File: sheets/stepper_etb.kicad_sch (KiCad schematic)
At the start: 12 parts, among them U202 DRV8825PWPR, U203 TLE9201SG

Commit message: Remediate power supply, main relay keep-alive, and schematic ERC to 0 errors
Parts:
- added D209: B340A-13-F, Diode_SMD:D_SMA, symbol Device:D_Schottky
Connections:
- net 12V_MR: now also D209.1 (K)
- net +3.3V renamed +3V3
- new net MAIN_RLY_CLAMP: D209.2 (A)
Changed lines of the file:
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@@
 		(dnp no)
 		(property "Reference" "#PWR0850" (at 48.26 38.1 0) (effects (font (size 1.27 1.27)) (hide yes)))
-		(property "Value" "+3.3V" (at 48.26 38.1 0) (effects (font (size 1.27 1.27))))
+		(property "Value" "+3V3" (at 48.26 38.1 0) (effects (font (size 1.27 1.27))))
 		(property "Footprint" "" (at 48.26 40.64 0) (effects (font (size 1.27 1.27)) (hide yes)))
 		(property "Datasheet" "" (at 48.26 40.64 0) (effects (font (size 1.27 1.27)) (hide yes)))
@@
 		(dnp no)
 		(property "Reference" "#PWR0851" (at 48.26 40.64 0) (effects (font (size 1.27 1.27)) (hide yes)))
-		(property "Value" "+3.3V" (at 48.26 40.64 0) (effects (font (size 1.27 1.27))))
+		(property "Value" "+3V3" (at 48.26 40.64 0) (effects (font (size 1.27 1.27))))
 		(property "Footprint" "" (at 48.26 43.18 0) (effects (font (size 1.27 1.27)) (hide yes)))
 		(property "Datasheet" "" (at 48.26 43.18 0) (effects (font (size 1.27 1.27)) (hide yes)))
@@
 		(dnp no)
 		(property "Reference" "#PWR0856" (at 74.93 99.05999999999999 0) (effects (font (size 1.27 1.27)) (hide yes)))
-		(property "Value" "+3.3V" (at 74.93 99.05999999999999 0) (effects (font (size 1.27 1.27))))
+		(property "Value" "+3V3" (at 74.93 99.05999999999999 0) (effects (font (size 1.27 1.27))))
 		(property "Footprint" "" (at 74.93 101.6 0) (effects (font (size 1.27 1.27)) (hide yes)))
 		(property "Datasheet" "" (at 74.93 101.6 0) (effects (font (size 1.27 1.27)) (hide yes)))
@@
 		(effects
 			(font
+				(size 1.27 1.27)
+			)
+			(justify left)
+		)
+	)
+	(symbol
+		(lib_id "Device:D_Schottky")
+		(at 139.7 111.76 0)
+		(unit 1)
+		(exclude_from_sim no)
+		(in_bom yes)
+		(on_board yes)
+		(dnp no)
+		(property "Reference" "D209" (at 139.7 109.22 0) (effects (font (size 1.27 1.27))))
+		(property "Value" "B340A-13-F" (at 139.7 114.3 0) (effects (font (size 1.27 1.27))))
+		(property "Footprint" "Diode_SMD:D_SMA" (at 139.7 111.76 0) (effects (font (size 1.27 1.27)) (hide yes)))
+		(property "LCSC" "C8598" (at 139.7 111.76 0) (effects (font (size 1.27 1.27)) (hide yes)))
+		(pin "1")
+		(pin "2")
+		(instances
+			(project "fome-mc" (path "/3b9c5ffd-e59b-402d-8c5e-052f7ca643a4/a1000000-0000-4000-8000-000000000002" (reference "D209") (unit 1)))
+		)
+	)
+	(wire
+		(pts
+			(xy 129.54 111.76) (xy 135.89 111.76)
+		)
+		(stroke
+			(width 0)
+			(type default)
+		)
+	)
+	(label "12V_MR"
+		(at 129.54 111.76 180)
+		(fields_autoplaced yes)
+		(effects
+			(font
+				(size 1.27 1.27)
+			)
+			(justify right bottom)
+		)
+	)
+	(wire
+		(pts
+			(xy 143.51 111.76) (xy 152.4 111.76)
+		)
+		(stroke
+			(width 0)
+			(type default)
+		)
+	)
+	(hierarchical_label "MAIN_RLY_CLAMP"
+		(shape passive)
+		(at 152.4 111.76 0)
+		(effects
+			(font

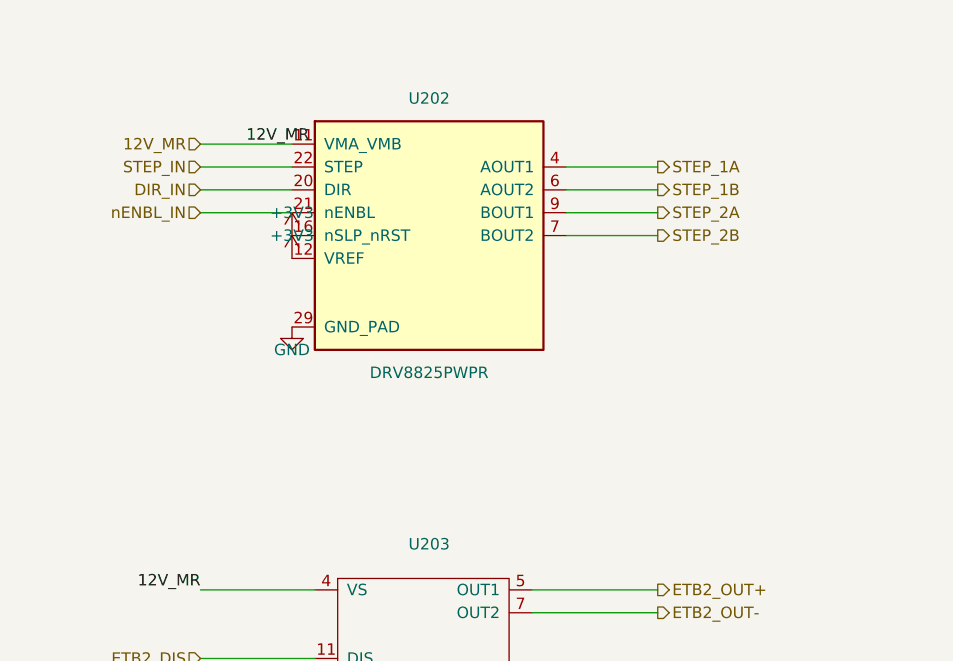
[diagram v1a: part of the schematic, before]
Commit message: Fix DRV8825PWPR (U202) HTSSOP-28 symbol pinout, VREF divider, charge pump, and 0.20R sense resistors (FOMEMC-5)
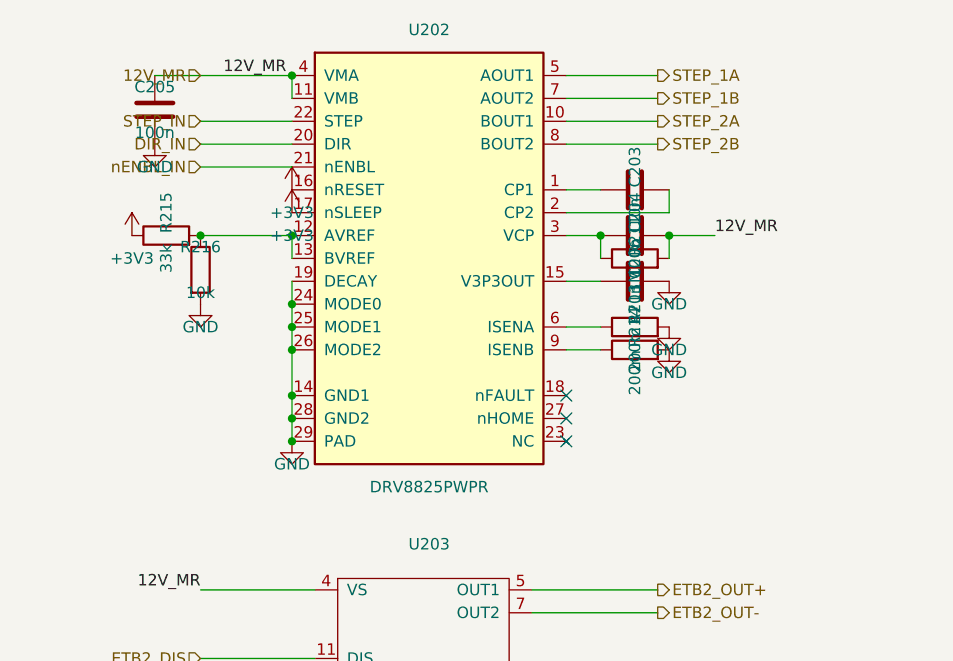
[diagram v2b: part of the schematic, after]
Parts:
- added C203: 10n, Capacitor_SMD:C_0603_1608Metric, symbol Device:C
- added C204, C205: 100n, Capacitor_SMD:C_0603_1608Metric, symbol Device:C
- added C206: 470n, Capacitor_SMD:C_0603_1608Metric, symbol Device:C
- added R211: 1M, Resistor_SMD:R_0603_1608Metric, symbol Device:R
- added R213, R214: 200m, Resistor_SMD:R_1206_3216Metric, symbol Device:R
- added R215: 33k, Resistor_SMD:R_0402_1005Metric, symbol Device:R
- added R216: 10k, Resistor_SMD:R_0402_1005Metric, symbol Device:R
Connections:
- net +3V3: now also U202.17 (nSLEEP), R215.1; no longer U202.12 (VREF)
- net 12V_MR: now also U202.4 (VMA), C204.2, C205.1, R211.2
- net GND: now also U202.14 (GND1), U202.19 (DECAY), U202.24 (MODE0), U202.25 (MODE1), U202.26 (MODE2), U202.28 (GND2), C205.2, C206.2, R213.2, R214.2, R216.2
- net STEP_1A: now also U202.5 (AOUT1); no longer U202.4 (AOUT1)
- net STEP_1B: now also U202.7 (AOUT2); no longer U202.6 (AOUT2)
- net STEP_2A: now also U202.10 (BOUT1); no longer U202.9 (BOUT1)
- net STEP_2B: now also U202.8 (BOUT2); no longer U202.7 (BOUT2)
- new net: R215.2, R216.1, U202.12 (AVREF), U202.13 (BVREF)
- new net: R214.1, U202.9 (ISENB)
- new net: C203.1, U202.1 (CP1)
- new net: C206.1, U202.15 (V3P3OUT)
- new net: C203.2, U202.2 (CP2)
- new net: C204.1, R211.1, U202.3 (VCP)
- new net: R213.1, U202.6 (ISENA)
- no-connect marks 4 -> 7

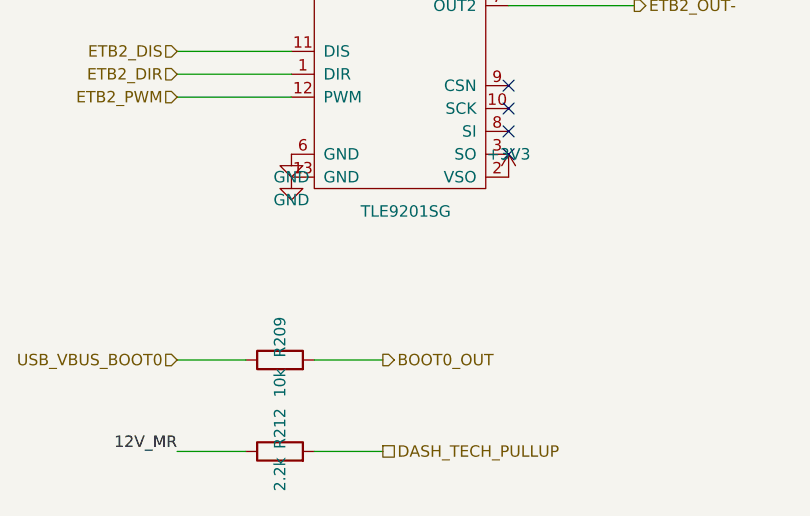
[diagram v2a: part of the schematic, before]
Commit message: Add D210 BZT52C6V8 BOOT0 threshold Zener, R217/R218/D211 PA9 VBUS sense divider/clamp, and SMCJ24A TVS protection on 12V_RAW and 12V_MR (FOMEMC-7)
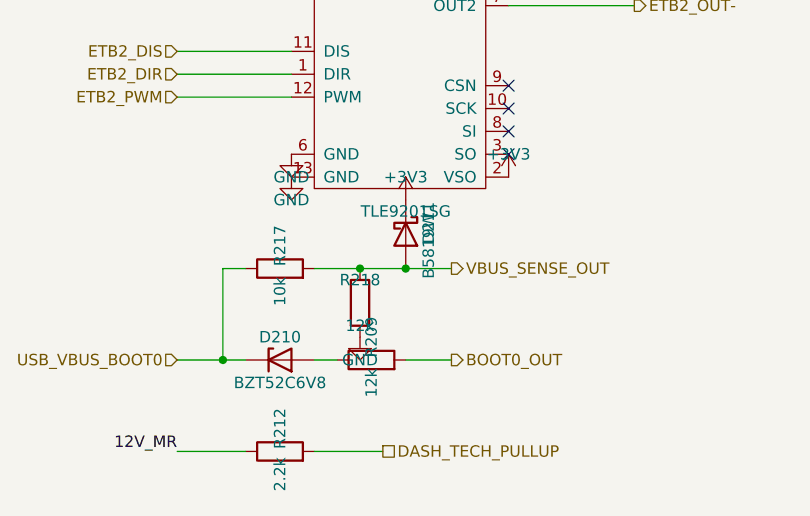
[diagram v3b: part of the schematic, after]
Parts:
- added D210: BZT52C6V8, Diode_SMD:D_SOD-123, symbol Device:D_Zener
- added D211: B5819W, Diode_SMD:D_SOD-123, symbol Device:D_Schottky
- added R217: 10k, Resistor_SMD:R_0402_1005Metric, symbol Device:R
- added R218: 12k, Resistor_SMD:R_0402_1005Metric, symbol Device:R
- R209: value 10k -> 12k; LCSC C25744 -> C25752
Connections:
- net +3V3: now also D211.1 (K)
- net GND: now also R218.2
- net USB_VBUS_BOOT0: now also D210.1 (K), R217.1; no longer R209.1
- new net: D210.2 (A), R209.1
- new net VBUS_SENSE_OUT: D211.2 (A), R217.2, R218.1
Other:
- moved on the sheet: R209
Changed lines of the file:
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@@
 	(wire
 		(pts
-			(xy 38.1 121.92) (xy 45.72 121.92)
+			(xy 38.1 121.92) (xy 43.18 121.92)
+		)
+		(stroke
+			(width 0)
+			(type default)
+		)
+	)
+	(wire
+		(pts
+			(xy 43.18 121.92) (xy 45.72 121.92)
+		)
+		(stroke
+			(width 0)
+			(type default)
+		)
+	)
+	(wire
+		(pts
+			(xy 43.18 121.92) (xy 43.18 111.76)
+		)
+		(stroke
+			(width 0)
+			(type default)
+		)
+	)
+	(wire
+		(pts
+			(xy 43.18 111.76) (xy 45.72 111.76)
+		)
+		(stroke
+			(width 0)
+			(type default)
+		)
+	)
+	(junction
+		(at 43.18 121.92)
+		(diameter 0)
+		(color 0 0 0 0)
+	)
+	(symbol
+		(lib_id "Device:D_Zener")
+		(at 49.53 121.92 0)
+		(unit 1)
+		(exclude_from_sim no)
+		(in_bom yes)
+		(on_board yes)
+		(dnp no)
+		(property "Reference" "D210" (at 49.53 119.38 0) (effects (font (size 1.27 1.27))))
+		(property "Value" "BZT52C6V8" (at 49.53 124.46 0) (effects (font (size 1.27 1.27))))
+		(property "Footprint" "Diode_SMD:D_SOD-123" (at 49.53 121.92 0) (effects (font (size 1.27 1.27)) (hide yes)))
+		(property "LCSC" "C173404" (at 49.53 121.92 0) (effects (font (size 1.27 1.27)) (hide yes)))
+		(pin "1")
+		(pin "2")
+		(instances
+			(project "fome-mc" (path "/3b9c5ffd-e59b-402d-8c5e-052f7ca643a4/a1000000-0000-4000-8000-000000000002" (reference "D210") (unit 1)))
+		)
+	)
+	(wire
+		(pts
+			(xy 53.34 121.92) (xy 55.88 121.92)
 		)
 		(stroke
@@
 	(symbol
 		(lib_id "Device:R")
-		(at 49.53 121.92 90)
-		(unit 1)
-		(exclude_from_sim no)
-		(in_bom yes)
-		(on_board yes)
-		(dnp no)
-		(property "Reference" "R209" (at 49.53 119.38 0) (effects (font (size 1.27 1.27))))
-		(property "Value" "10k" (at 49.53 124.46 0) (effects (font (size 1.27 1.27))))
-		(property "Footprint" "Resistor_SMD:R_0402_1005Metric" (at 49.53 121.92 0) (effects (font (size 1.27 1.27)) (hide yes)))
-		(property "LCSC" "C25744" (at 49.53 121.92 0) (effects (font (size 1.27 1.27)) (hide yes)))
+		(at 59.69 121.92 90)
+		(unit 1)
+		(exclude_from_sim no)
+		(in_bom yes)
+		(on_board yes)
+		(dnp no)
+		(property "Reference" "R209" (at 59.69 119.38 0) (effects (font (size 1.27 1.27))))
+		(property "Value" "12k" (at 59.69 124.46 0) (effects (font (size 1.27 1.27))))
+		(property "Footprint" "Resistor_SMD:R_0402_1005Metric" (at 59.69 121.92 0) (effects (font (size 1.27 1.27)) (hide yes)))
+		(property "LCSC" "C25752" (at 59.69 121.92 0) (effects (font (size 1.27 1.27)) (hide yes)))
 		(pin "1")
 		(pin "2")
 		(instances
 			(project "fome-mc" (path "/3b9c5ffd-e59b-402d-8c5e-052f7ca643a4/a1000000-0000-4000-8000-000000000002" (reference "R209") (unit 1)))
-			(project "fome-mc" (path "/3b9c5ffd-e59b-402d-8c5e-052f7ca643a4/a1000000-0000-4000-8000-000000000002" (reference "R209") (unit 1)))
-		)
-	)
-	(wire
-		(pts
-			(xy 53.34 121.92) (xy 60.96 121.92)
+		)
+	)
+	(wire
+		(pts
+			(xy 63.5 121.92) (xy 68.58 121.92)
 		)
 		(stroke
@@
 	(hierarchical_label "BOOT0_OUT"
 		(shape output)
-		(at 60.96 121.92 0)
+		(at 68.58 121.92 0)
 		(effects
 			(font
+				(size 1.27 1.27)
+			)
+			(justify left)
+		)
+	)
+	(symbol
+		(lib_id "Device:R")
+		(at 49.53 111.76 90)
+		(unit 1)
+		(exclude_from_sim no)
+		(in_bom yes)
+		(on_board yes)
+		(dnp no)
+		(property "Reference" "R217" (at 49.53 109.22 0) (effects (font (size 1.27 1.27))))
+		(property "Value" "10k" (at 49.53 114.3 0) (effects (font (size 1.27 1.27))))
+		(property "Footprint" "Resistor_SMD:R_0402_1005Metric" (at 49.53 111.76 0) (effects (font (size 1.27 1.27)) (hide yes)))
+		(property "LCSC" "C25744" (at 49.53 111.76 0) (effects (font (size 1.27 1.27)) (hide yes)))
+		(pin "1")
+		(pin "2")
+		(instances
+			(project "fome-mc" (path "/3b9c5ffd-e59b-402d-8c5e-052f7ca643a4/a1000000-0000-4000-8000-000000000002" (reference "R217") (unit 1)))
+		)
+	)
+	(wire
+		(pts
+			(xy 53.34 111.76) (xy 58.42 111.76)
+		)
+		(stroke
+			(width 0)
+			(type default)
+		)
+	)
+	(wire
+		(pts
+			(xy 58.42 111.76) (xy 63.5 111.76)
+		)
+		(stroke
+			(width 0)
+			(type default)
+		)
+	)
+	(wire
+		(pts
+			(xy 63.5 111.76) (xy 68.58 111.76)
+		)
+		(stroke
+			(width 0)
+			(type default)
+		)
+	)
+	(junction
+		(at 58.42 111.76)
+		(diameter 0)
+		(color 0 0 0 0)
+	)
+	(junction
+		(at 63.5 111.76)
+		(diameter 0)
+		(color 0 0 0 0)
+	)
+	(symbol
+		(lib_id "Device:R")
+		(at 58.42 115.57 0)
+		(unit 1)
+		(exclude_from_sim no)
+		(in_bom yes)
+		(on_board yes)
+		(dnp no)
+		(property "Reference" "R218" (at 58.42 113.03 0) (effects (font (size 1.27 1.27))))
+		(property "Value" "12k" (at 58.42 118.11 0) (effects (font (size 1.27 1.27))))
+		(property "Footprint" "Resistor_SMD:R_0402_1005Metric" (at 58.42 115.57 0) (effects (font (size 1.27 1.27)) (hide yes)))
+		(property "LCSC" "C25752" (at 58.42 115.57 0) (effects (font (size 1.27 1.27)) (hide yes)))
+		(pin "1")
+		(pin "2")
+		(instances
+			(project "fome-mc" (path "/3b9c5ffd-e59b-402d-8c5e-052f7ca643a4/a1000000-0000-4000-8000-000000000002" (reference "R218") (unit 1)))
+		)
+	)
+	(symbol
+		(lib_id "power:GND")
+		(at 58.42 119.38 0)
+		(unit 1)
+		(exclude_from_sim no)
+		(in_bom yes)
+		(on_board yes)
+		(dnp no)
+		(property "Reference" "#PWR0861" (at 58.42 121.92 0) (effects (font (size 1.27 1.27)) (hide yes)))
+		(property "Value" "GND" (at 58.42 121.92 0) (effects (font (size 1.27 1.27))))
+		(property "Footprint" "" (at 58.42 119.38 0) (effects (font (size 1.27 1.27)) (hide yes)))
+		(property "Datasheet" "" (at 58.42 119.38 0) (effects (font (size 1.27 1.27)) (hide yes)))
+		(pin "1")
+		(instances
+			(project "fome-mc" (path "/3b9c5ffd-e59b-402d-8c5e-052f7ca643a4/a1000000-0000-4000-8000-000000000002" (reference "#PWR0861") (unit 1)))
+		)
+	)
+	(symbol
+		(lib_id "Device:D_Schottky")
+		(at 63.5 107.95 270)
+		(unit 1)
+		(exclude_from_sim no)
+		(in_bom yes)
+		(on_board yes)
+		(dnp no)
+		(property "Reference" "D211" (at 66.04 106.68 0) (effects (font (size 1.27 1.27))))
+		(property "Value" "B5819W" (at 66.04 109.22 0) (effects (font (size 1.27 1.27))))
+		(property "Footprint" "Diode_SMD:D_SOD-123" (at 63.5 107.95 0) (effects (font (size 1.27 1.27)) (hide yes)))
+		(property "LCSC" "C8598" (at 63.5 107.95 0) (effects (font (size 1.27 1.27)) (hide yes)))
+		(pin "1")
+		(pin "2")
+		(instances
+			(project "fome-mc" (path "/3b9c5ffd-e59b-402d-8c5e-052f7ca643a4/a1000000-0000-4000-8000-000000000002" (reference "D211") (unit 1)))
+		)
+	)
+	(symbol
+		(lib_id "power:+3.3V")
+		(at 63.5 104.14 0)
+		(unit 1)
+		(exclude_from_sim no)
+		(in_bom yes)
+		(on_board yes)
+		(dnp no)
+		(property "Reference" "#PWR0862" (at 63.5 101.6 0) (effects (font (size 1.27 1.27)) (hide yes)))
+		(property "Value" "+3V3" (at 63.5 101.6 0) (effects (font (size 1.27 1.27))))
+		(property "Footprint" "" (at 63.5 104.14 0) (effects (font (size 1.27 1.27)) (hide yes)))
+		(property "Datasheet" "" (at 63.5 104.14 0) (effects (font (size 1.27 1.27)) (hide yes)))
+		(pin "1")
+		(instances
+			(project "fome-mc" (path "/3b9c5ffd-e59b-402d-8c5e-052f7ca643a4/a1000000-0000-4000-8000-000000000002" (reference "#PWR0862") (unit 1)))
+		)
+	)
+	(hierarchical_label "VBUS_SENSE_OUT"
+		(shape output)
+		(at 68.58 111.76 0)
+		(effects
+			(font

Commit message: Add SDMMC1 47k pull-ups (R127..R131) & 22R clock damping (R132), mark U24 LPS25HB DNP, fix B340A/B5819W LCSC codes, and reconcile docs/verify_io_map (FOMEMC-8)
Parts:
- D201, D202, D203, D204, D205, D206, D207, D208, D209: LCSC C8598 -> C64982
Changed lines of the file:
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@@
 		(property "Value" "B340A-13-F" (at 139.7 33.02 0) (effects (font (size 1.27 1.27))))
 		(property "Footprint" "Diode_SMD:D_SMA" (at 139.7 30.48 0) (effects (font (size 1.27 1.27)) (hide yes)))
-		(property "LCSC" "C8598" (at 139.7 30.48 0) (effects (font (size 1.27 1.27)) (hide yes)))
+		(property "LCSC" "C64982" (at 139.7 30.48 0) (effects (font (size 1.27 1.27)) (hide yes)))
 		(pin "1")
 		(pin "2")
@@
 		(property "Value" "B340A-13-F" (at 139.7 43.18 0) (effects (font (size 1.27 1.27))))
 		(property "Footprint" "Diode_SMD:D_SMA" (at 139.7 40.64 0) (effects (font (size 1.27 1.27)) (hide yes)))
-		(property "LCSC" "C8598" (at 139.7 40.64 0) (effects (font (size 1.27 1.27)) (hide yes)))
+		(property "LCSC" "C64982" (at 139.7 40.64 0) (effects (font (size 1.27 1.27)) (hide yes)))
 		(pin "1")
 		(pin "2")
@@
 		(property "Value" "B340A-13-F" (at 139.7 53.339999999999996 0) (effects (font (size 1.27 1.27))))
 		(property "Footprint" "Diode_SMD:D_SMA" (at 139.7 50.8 0) (effects (font (size 1.27 1.27)) (hide yes)))
-		(property "LCSC" "C8598" (at 139.7 50.8 0) (effects (font (size 1.27 1.27)) (hide yes)))
+		(property "LCSC" "C64982" (at 139.7 50.8 0) (effects (font (size 1.27 1.27)) (hide yes)))
 		(pin "1")
 		(pin "2")
@@
 		(property "Value" "B340A-13-F" (at 139.7 63.5 0) (effects (font (size 1.27 1.27))))
 		(property "Footprint" "Diode_SMD:D_SMA" (at 139.7 60.96 0) (effects (font (size 1.27 1.27)) (hide yes)))
-		(property "LCSC" "C8598" (at 139.7 60.96 0) (effects (font (size 1.27 1.27)) (hide yes)))
+		(property "LCSC" "C64982" (at 139.7 60.96 0) (effects (font (size 1.27 1.27)) (hide yes)))
 		(pin "1")
 		(pin "2")
@@
 		(property "Value" "B340A-13-F" (at 139.7 73.66000000000001 0) (effects (font (size 1.27 1.27))))
 		(property "Footprint" "Diode_SMD:D_SMA" (at 139.7 71.12 0) (effects (font (size 1.27 1.27)) (hide yes)))
-		(property "LCSC" "C8598" (at 139.7 71.12 0) (effects (font (size 1.27 1.27)) (hide yes)))
+		(property "LCSC" "C64982" (at 139.7 71.12 0) (effects (font (size 1.27 1.27)) (hide yes)))
 		(pin "1")
 		(pin "2")
@@
 		(property "Value" "B340A-13-F" (at 139.7 83.82000000000001 0) (effects (font (size 1.27 1.27))))
 		(property "Footprint" "Diode_SMD:D_SMA" (at 139.7 81.28 0) (effects (font (size 1.27 1.27)) (hide yes)))
-		(property "LCSC" "C8598" (at 139.7 81.28 0) (effects (font (size 1.27 1.27)) (hide yes)))
+		(property "LCSC" "C64982" (at 139.7 81.28 0) (effects (font (size 1.27 1.27)) (hide yes)))
 		(pin "1")
 		(pin "2")
@@
 		(property "Value" "B340A-13-F" (at 139.7 93.98 0) (effects (font (size 1.27 1.27))))
 		(property "Footprint" "Diode_SMD:D_SMA" (at 139.7 91.44 0) (effects (font (size 1.27 1.27)) (hide yes)))
-		(property "LCSC" "C8598" (at 139.7 91.44 0) (effects (font (size 1.27 1.27)) (hide yes)))
+		(property "LCSC" "C64982" (at 139.7 91.44 0) (effects (font (size 1.27 1.27)) (hide yes)))
 		(pin "1")
 		(pin "2")
@@
 		(property "Value" "B340A-13-F" (at 139.7 104.14000000000001 0) (effects (font (size 1.27 1.27))))
 		(property "Footprint" "Diode_SMD:D_SMA" (at 139.7 101.60000000000001 0) (effects (font (size 1.27 1.27)) (hide yes)))
-		(property "LCSC" "C8598" (at 139.7 101.60000000000001 0) (effects (font (size 1.27 1.27)) (hide yes)))
+		(property "LCSC" "C64982" (at 139.7 101.60000000000001 0) (effects (font (size 1.27 1.27)) (hide yes)))
 		(pin "1")
 		(pin "2")
@@
 		(property "Value" "B340A-13-F" (at 139.7 114.3 0) (effects (font (size 1.27 1.27))))
 		(property "Footprint" "Diode_SMD:D_SMA" (at 139.7 111.76 0) (effects (font (size 1.27 1.27)) (hide yes)))
-		(property "LCSC" "C8598" (at 139.7 111.76 0) (effects (font (size 1.27 1.27)) (hide yes)))
-		(pin "1")
-		(pin "2")
+		(property "LCSC" "C64982" (at 139.7 111.76 0) (effects (font (size 1.27 1.27)) (hide yes)))
+		(pin "1")
+		(pin "2")
